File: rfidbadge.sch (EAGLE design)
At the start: 57 parts, among them Q1 BSS123, U1 ATMEGA328P_TQFP, U2 CLRC663, Y1 27.12 MHz

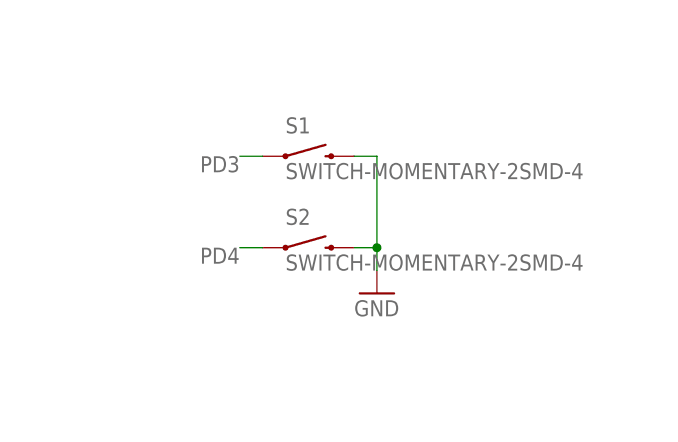
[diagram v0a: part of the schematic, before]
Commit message: Add reset switch
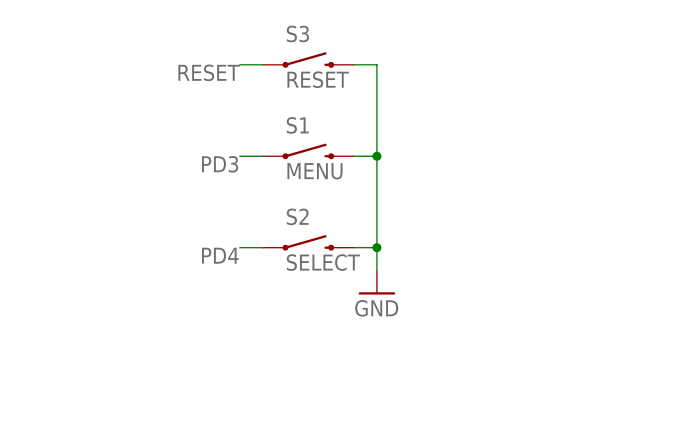
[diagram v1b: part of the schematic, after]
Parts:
- added S3: RESET, SparkFun-Electromechanical:SWITCH-MOMENTARY-2SMD-1101NE
- S1: value SWITCH-MOMENTARY-2SMD-4 -> MENU
- S2: value SWITCH-MOMENTARY-2SMD-4 -> SELECT
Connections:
- net GND: now also S3.2
- net RESET: now also S3.1
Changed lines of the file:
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@@
 <part name="GND10" library="supply1" deviceset="GND" device=""/>
 <part name="VDD6" library="supply1" deviceset="VDD" device=""/>
-<part name="S1" library="SparkFun-Electromechanical" deviceset="SWITCH-MOMENTARY-2" device="SMD-4">
+<part name="S1" library="SparkFun-Electromechanical" deviceset="SWITCH-MOMENTARY-2" device="SMD-4" value="MENU">
 <attribute name="PROD_ID" value="CKN9112CT-ND"/>
 </part>
-<part name="S2" library="SparkFun-Electromechanical" deviceset="SWITCH-MOMENTARY-2" device="SMD-4">
+<part name="S2" library="SparkFun-Electromechanical" deviceset="SWITCH-MOMENTARY-2" device="SMD-4" value="SELECT">
 <attribute name="PROD_ID" value="CKN9112CT-ND"/>
 </part>
@@
 <part name="TP5" library="testpad" deviceset="TP" device="TP06R" value="TPTP06R"/>
 <part name="TP6" library="testpad" deviceset="TP" device="TP06R" value="TPTP06R"/>
+<part name="S3" library="SparkFun-Electromechanical" deviceset="SWITCH-MOMENTARY-2" device="SMD-1101NE" value="RESET">
+<attribute name="PROD_ID" value="CKN10388CT-ND"/>
+</part>
 </parts>
 <sheets>
@@
 <instance part="TP5" gate="G$1" x="63.5" y="22.86" rot="R90"/>
 <instance part="TP6" gate="G$1" x="63.5" y="20.32" rot="R90"/>
+<instance part="S3" gate="G$1" x="157.48" y="91.44"/>
 </instances>
 <busses>
@@
 <wire x1="162.56" y1="71.12" x2="165.1" y2="71.12" width="0.1524" layer="91"/>
 <junction x="165.1" y="71.12"/>
+<pinref part="S3" gate="G$1" pin="2"/>
+<wire x1="162.56" y1="91.44" x2="165.1" y2="91.44" width="0.1524" layer="91"/>
+<wire x1="165.1" y1="91.44" x2="165.1" y2="81.28" width="0.1524" layer="91"/>
+<junction x="165.1" y="81.28"/>
 </segment>
 </net>
@@
 <label x="7.62" y="-45.72" size="1.778" layer="95"/>
 </segment>
-</net>
+<segment>
+<pinref part="S3" gate="G$1" pin="1"/>
+<wire x1="152.4" y1="91.44" x2="149.86" y2="91.44" width="0.1524" layer="91"/>
+<label x="149.86" y="91.44" size="1.778" layer="95" rot="R180"/>
+</segment>
+</net>

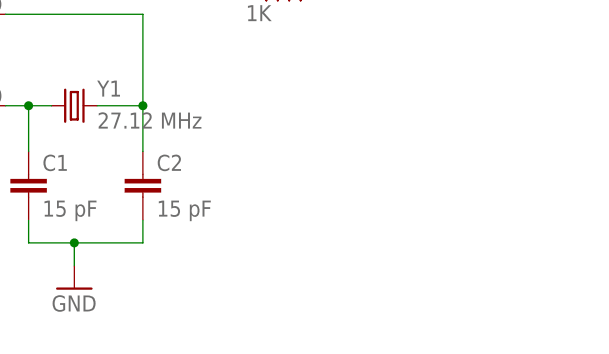
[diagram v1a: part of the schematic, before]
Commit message: Add Defcon 24 logo
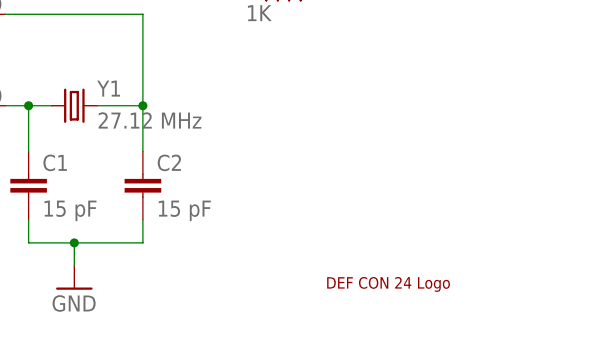
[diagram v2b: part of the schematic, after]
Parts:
- added U$1: DC24LOGO, artwork:DC24LOGO
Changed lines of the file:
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@@
 <attribute name="PROD_ID" value="CKN10388CT-ND"/>
 </part>
+<part name="U$1" library="artwork" deviceset="DC24LOGO" device=""/>
 </parts>
 <sheets>
@@
 <instance part="TP6" gate="G$1" x="63.5" y="20.32" rot="R90"/>
 <instance part="S3" gate="G$1" x="157.48" y="91.44"/>
+<instance part="U$1" gate="G$1" x="154.94" y="-58.42"/>
 </instances>
 <busses>
